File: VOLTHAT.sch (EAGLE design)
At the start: 25 parts, among them IC2 EUP3476SO08T, J1 DC IN

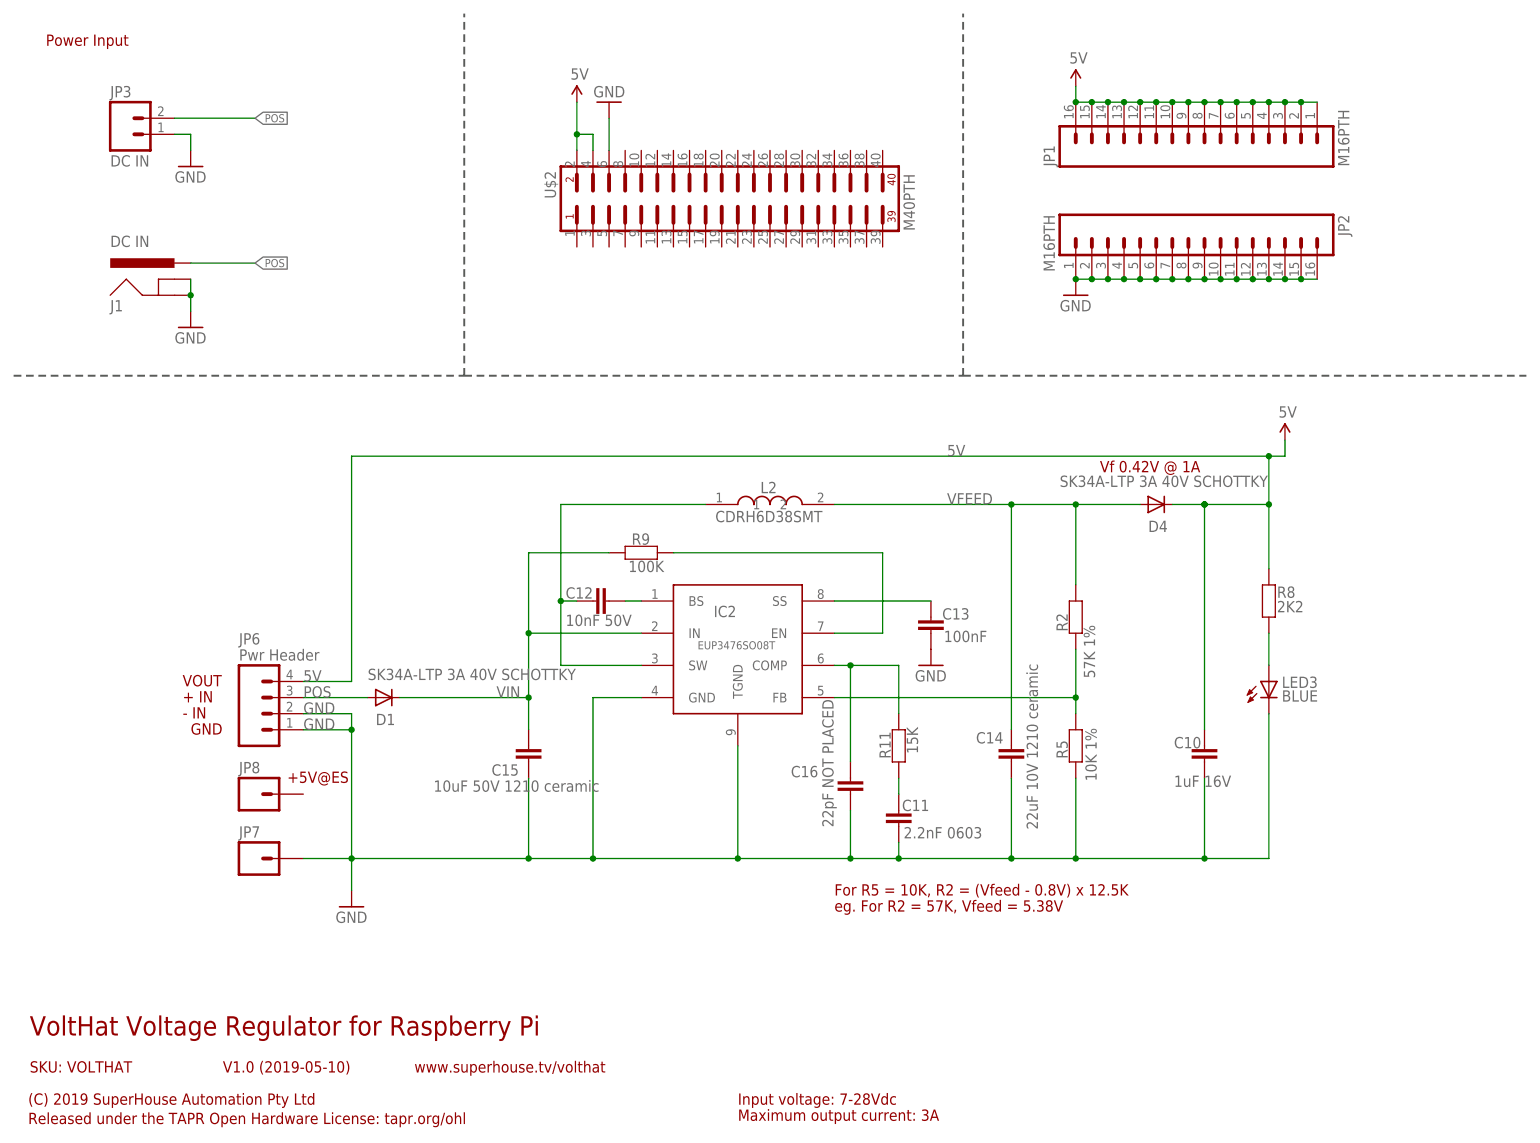
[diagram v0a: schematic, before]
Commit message: Added header to take power from PoE on Raspberry Pi 3 B+
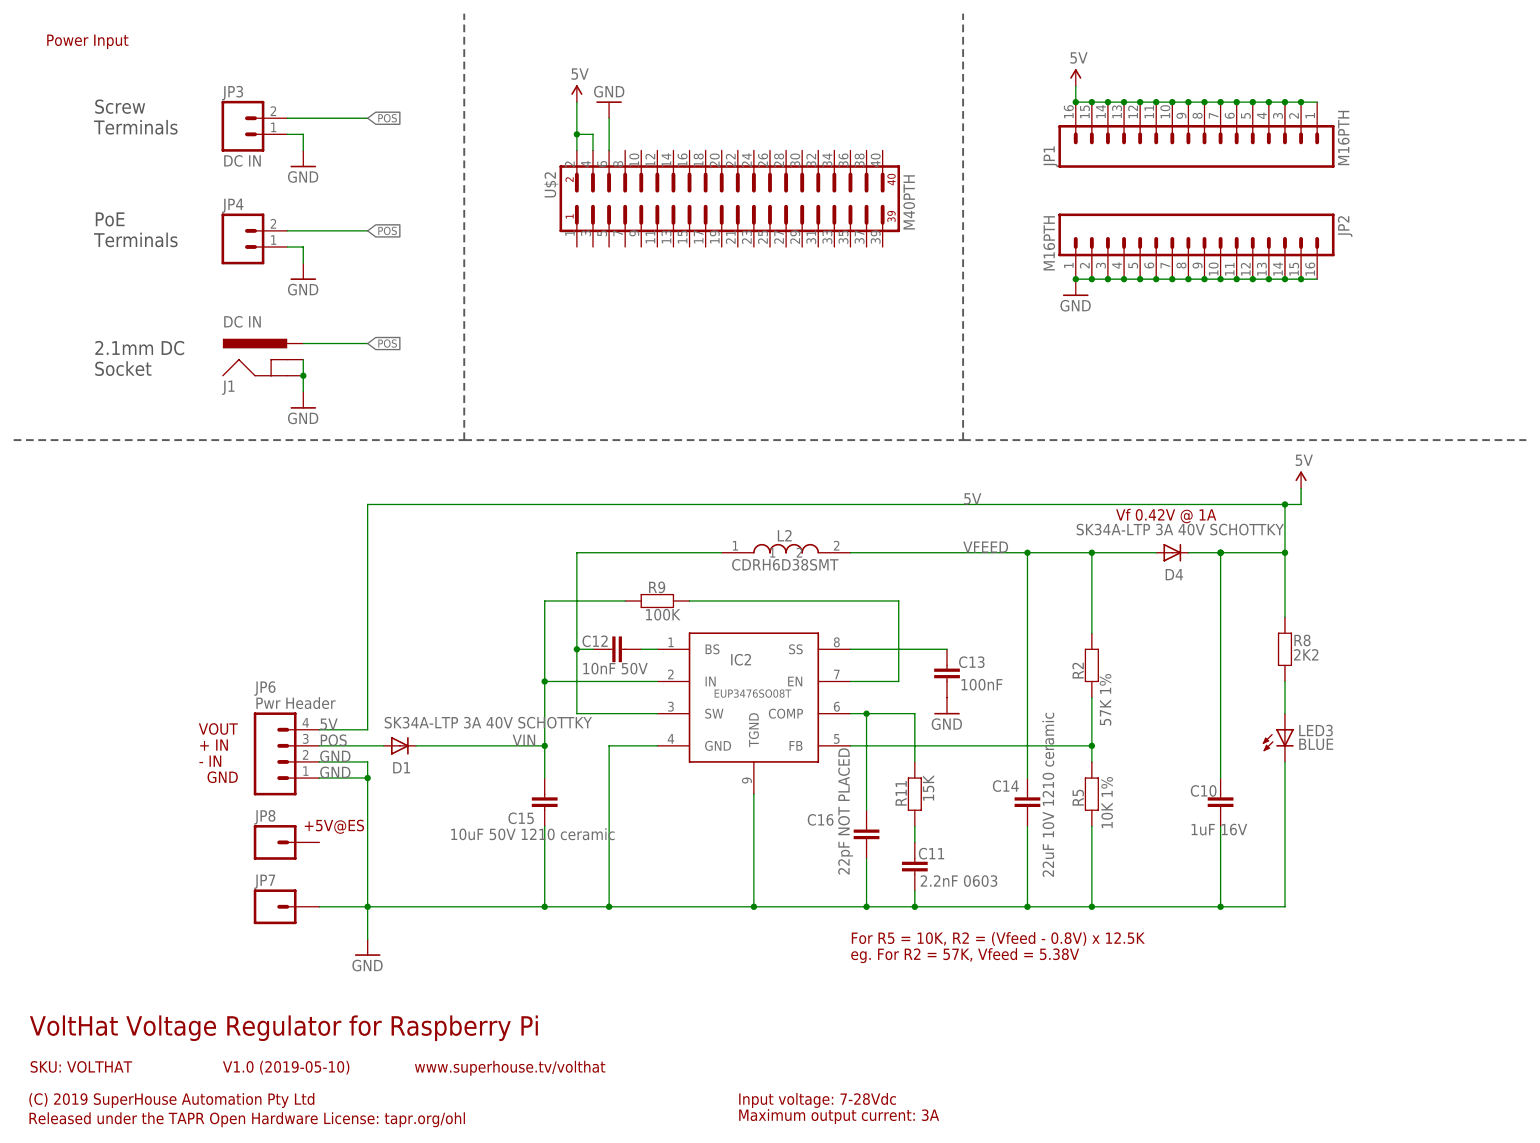
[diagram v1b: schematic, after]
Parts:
- added JP4: (no value), freetronics-jon:M02PTH
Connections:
- net GND: now also JP4.1
- net POS: now also JP4.2
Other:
- note added: "2.1mm DC Socket"
- note added: "PoE Terminals"
- note added: "Screw Terminals"
- moved on the sheet: C10, C11, C12, C13, C14, C15, C16, D1, D4, IC2, J1, JP3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

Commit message: Major routing for v1.0 release
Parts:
- removed JP2: M16PTH, freetronics-jon:M16PTH
- added JP10: OLED, freetronics-jon:M04PTH
- added JP9: M14PTH, freetronics-jon:M14PTH
- added SJ1, SJ2: (no value), freetronics-jon:SJN
- JP1: value M16PTH -> M14PTH; device freetronics-jon:M16PTH -> freetronics-jon:M14PTH
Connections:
- new net 3.3V: JP10.3, U$2.1
- new net N$1: JP4.1, SJ2.1
- new net N$2: JP4.2, SJ1.1
- new net SCL: JP10.2, U$2.5
- new net SDA: JP10.1, U$2.3
- net 5V: now also JP9.1, JP9.10, JP9.11, JP9.12, JP9.13, JP9.14, JP9.2, JP9.3, JP9.4, JP9.5, JP9.6, JP9.7, JP9.8, JP9.9; no longer JP1.1, JP1.10, JP1.11, JP1.12, JP1.13, JP1.14, JP1.15, JP1.16, JP1.2, JP1.3, JP1.4, JP1.5, JP1.6, JP1.7, JP1.8, JP1.9
- net GND: now also JP1.1, JP1.10, JP1.11, JP1.12, JP1.13, JP1.14, JP1.2, JP1.3, JP1.4, JP1.5, JP1.6, JP1.7, JP1.8, JP1.9, JP10.4, SJ2.2, U$2.14, U$2.20, U$2.25, U$2.30, U$2.39, U$2.9; no longer JP2.1, JP2.10, JP2.11, JP2.12, JP2.13, JP2.14, JP2.15, JP2.16, JP2.2, JP2.3, JP2.4, JP2.5, JP2.6, JP2.7, JP2.8, JP2.9, JP4.1
- net POS: now also SJ1.2; no longer JP4.2
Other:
- note added: "I2C OLED Header"
- note added: "PoE Header"
- note added: "Power Rails"
- note added: "Raspberry Pi Header"
- note added: "Voltage Regulator"
- note removed: "PoE Terminals"
- moved on the sheet: C10, C11, C12, C13, C14, C15, C16, D1, D4, IC2, J1, JP3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

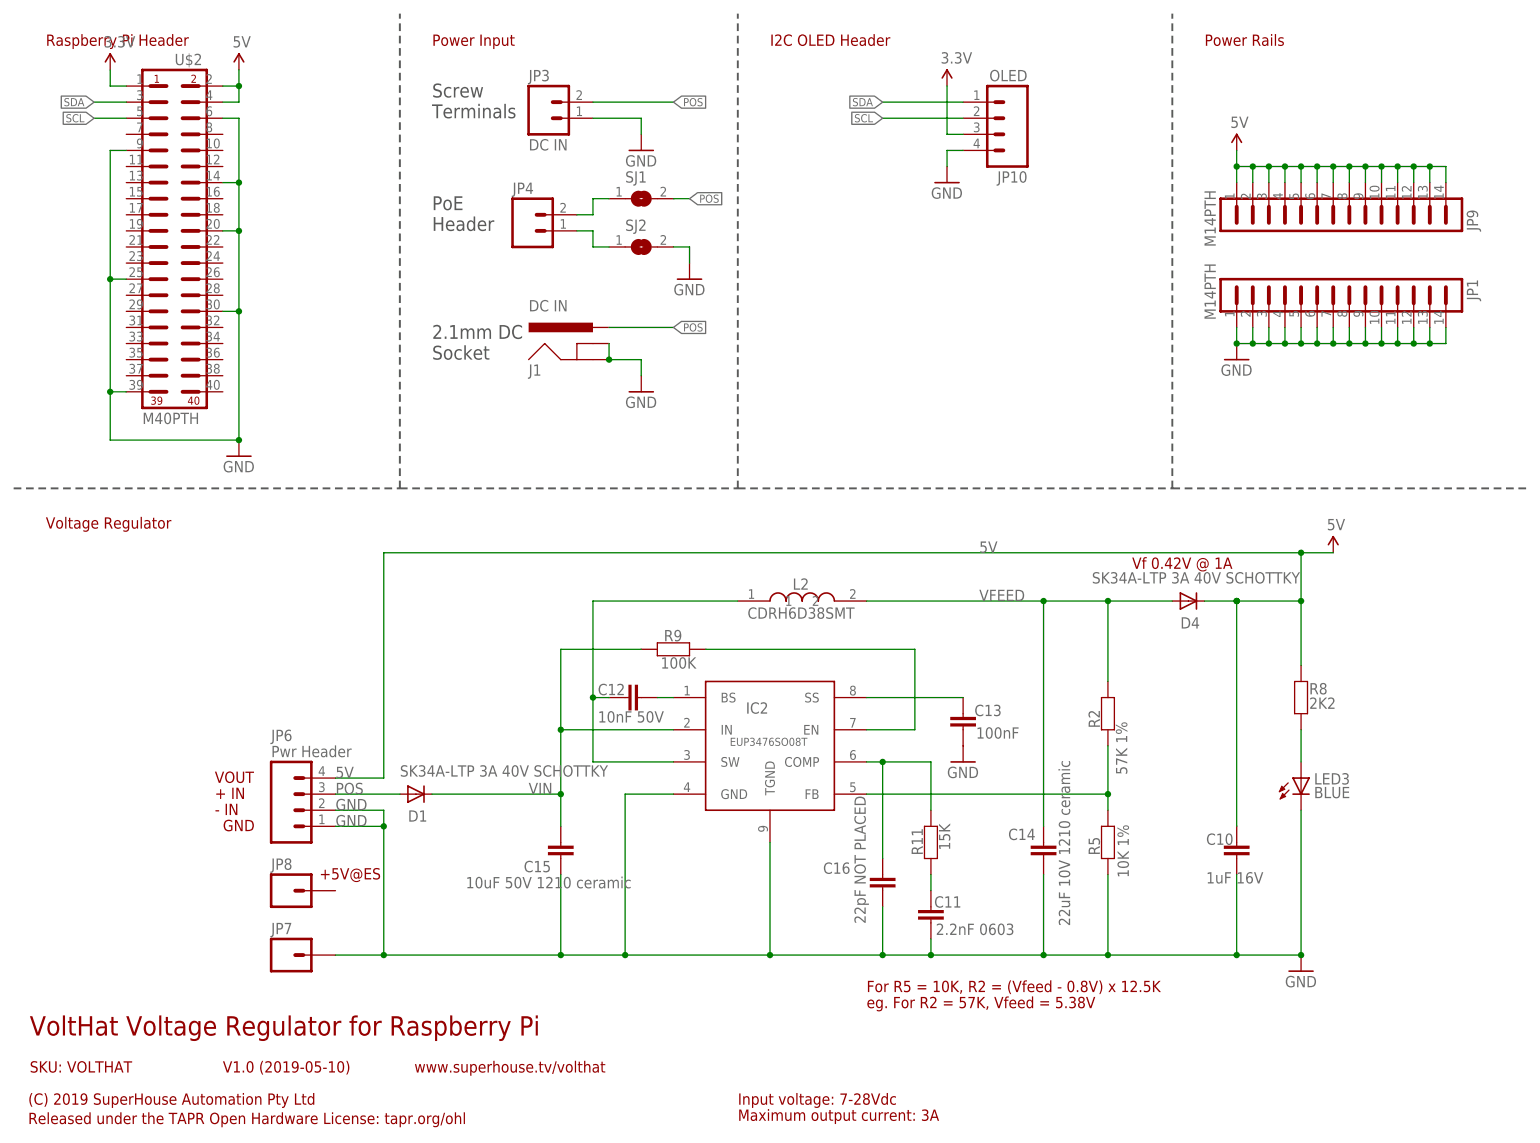
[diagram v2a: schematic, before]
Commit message: Major rework with 3A regulator module for v2.0 release
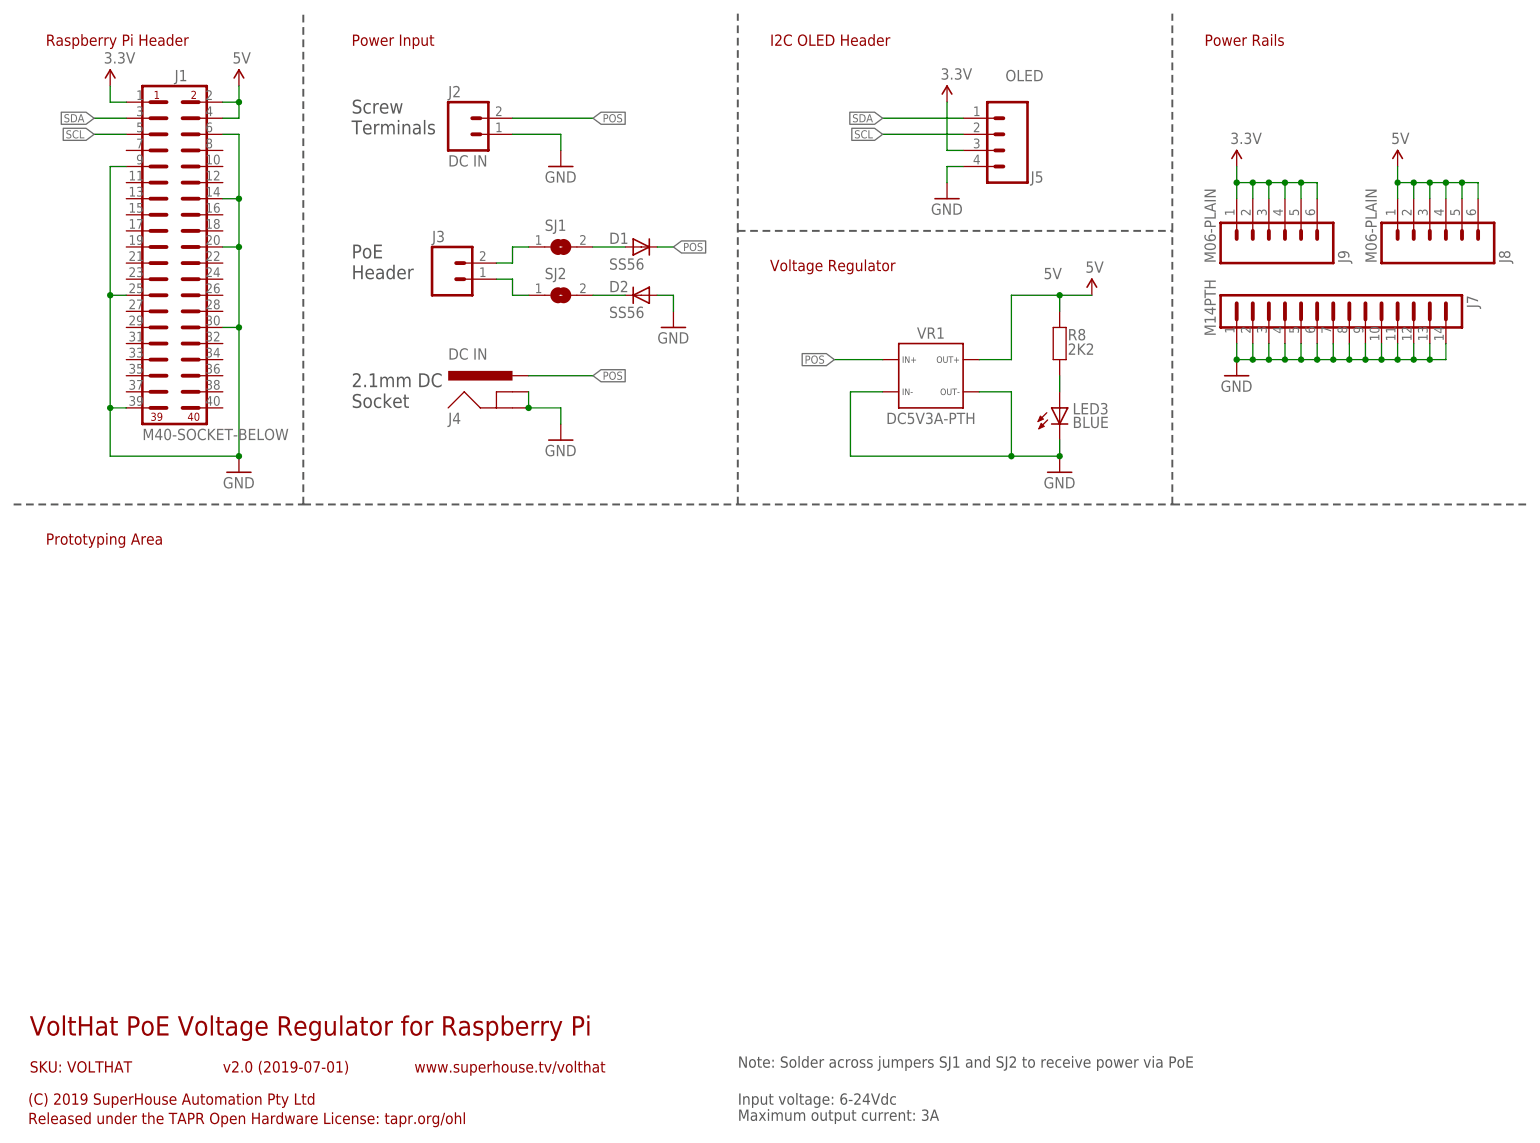
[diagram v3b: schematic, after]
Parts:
- removed C10: 1uF 16V, freetronics:CAP0603
- removed C11: 2.2nF 0603, freetronics-marc:CAP0603
- removed C12: 10nF 50V, freetronics-marc:CAP0603
- removed C13: 100nF, freetronics-marc:CAP0603
- removed C14: 22uF 10V 1210 ceramic, freetronics-jon:C-EUC1210
- removed C15: 10uF 50V 1210 ceramic, freetronics-jon:C-EUC1210
- removed C16: 22pF NOT PLACED, freetronics-marc:CAP0603
- removed D4: SK34A-LTP 3A 40V SCHOTTKY, freetronics-master-v1:DIODESMA
- removed IC2: EUP3476SO08T, freetronics-jon:EUP3476SO08T
- removed JP1, JP9: M14PTH, freetronics-jon:M14PTH
- removed JP10: OLED, freetronics-jon:M04PTH
- removed JP3: DC IN, freetronics-jon:M023.5MM
- removed JP4: (no value), freetronics-jon:M02PTH
- removed JP6: Pwr Header, freetronics:M04PTH
- removed JP7, JP8: M01PTH, freetronics:M01PTH
- removed L2: CDRH6D38SMT, freetronics-jon:CDRH6D38SMT
- removed R11: 15K, freetronics-marc:RESISTOR0603
- removed R2: 57K 1%, freetronics-marc:RESISTOR0603
- removed R5: 10K 1%, freetronics-marc:RESISTOR0603
- removed R9: 100K, freetronics-marc:RESISTOR0603
- removed U$2: M40PTH, freetronics-jon:M40PTH
- added D2: SS56, SuperHouse-DiscreteSemi:DIODESMA
- added J2: DC IN, SuperHouse-Connectors:M02-SCREW-3.5MM
- added J3: (no value), SuperHouse-Connectors:M02-SOCKET-BELOW
- added J4: DC IN, SuperHouse-Connectors:POWER_JACK-SLOTS
- added J5: OLED, SuperHouse-Connectors:M04-PLAIN
- added J7: M14PTH, freetronics-jon:M14PTH
- added J8, J9: M06-PLAIN, SuperHouse-Connectors:M06-PLAIN
- added VR1: DC5V3A-PTH, SuperHouse-Regulators:DC5V3A-PTH
- D1: value SK34A-LTP 3A 40V SCHOTTKY -> SS56; device freetronics-master-v1:DIODESMA -> SuperHouse-DiscreteSemi:DIODESMA
- J1: value DC IN -> M40-SOCKET-BELOW; device freetronics-jon:POWER_JACKPTH_SLOTS -> SuperHouse-Connectors:M40-SOCKET-BELOW
- LED3: device freetronics:LED0603 -> SuperHouse-LEDs:LED0603
- R8: device freetronics:RESISTOR0603 -> SuperHouse-DiscreteSemi:RESISTOR0603
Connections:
- removed net N$204: IC2.EN, R9.1
- removed net N$205: IC2.FB, R2.2, R5.2
- removed net N$206: C16.1, IC2.COMP, R11.2
- removed net N$207: C11.1, R11.1
- removed net N$208: C12.2, IC2.BS
- removed net N$209: C13.2, IC2.SS
- removed net N$210: C12.1, IC2.SW, L2.1
- removed net VFEED: C14.1, D4.A, L2.2, R2.1
- removed net VIN: C15.1, D1.C, IC2.IN, R9.2
- new net N$24: D1.A, SJ1.2
- new net N$25: D2.C, SJ2.2
- net 3.3V: now also J1.1, J5.3, J9.1, J9.2, J9.3, J9.4, J9.5, J9.6; no longer JP10.3, U$2.1
- net 5V: now also J1.2, J1.4, J8.1, J8.2, J8.3, J8.4, J8.5, J8.6, VR1.3; no longer C10.1, D4.C, JP6.4, JP9.1, JP9.10, JP9.11, JP9.12, JP9.13, JP9.14, JP9.2, JP9.3, JP9.4, JP9.5, JP9.6, JP9.7, JP9.8, JP9.9, U$2.2, U$2.4
- net GND: now also D2.A, J1.14, J1.20, J1.25, J1.30, J1.39, J1.6, J1.9, J2.1, J4.GND, J4.GNDBREAK, J5.4, J7.1, J7.10, J7.11, J7.12, J7.13, J7.14, J7.2, J7.3, J7.4, J7.5, J7.6, J7.7, J7.8, J7.9, VR1.1, VR1.4; no longer C10.2, C11.2, C13.1, C14.2, C15.2, C16.2, IC2.GND, IC2.TGND, J1.GND, J1.GNDBREAK, JP1.1, JP1.10, JP1.11, JP1.12, JP1.13, JP1.14, JP1.2, JP1.3, JP1.4, JP1.5, JP1.6, JP1.7, JP1.8, JP1.9, JP10.4, JP3.1, JP6.1, JP6.2, JP7.1, R5.1, SJ2.2, U$2.14, U$2.20, U$2.25, U$2.30, U$2.39, U$2.6, U$2.9
- net N$1: now also J3.1; no longer JP4.1
- net N$2: now also J3.2; no longer JP4.2
- net POS: now also D1.C, J2.2, J4.PWR, VR1.2; no longer D1.A, J1.PWR, JP3.2, JP6.3, SJ1.2
- net SCL: now also J1.5, J5.2; no longer JP10.2, U$2.5
- net SDA: now also J1.3, J5.1; no longer JP10.1, U$2.3
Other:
- note added: "Input voltage: 6-24Vdc"
- note added: "Note: Solder across jumpers SJ1 and SJ2 to receive power via PoE"
- note added: "Prototyping Area"
- note added: "VoltHat PoE Voltage Regulator for Raspberry Pi"
- note added: "v2.0 (2019-07-01)"
- note removed: "+ IN"
- note removed: "+5V@ES"
- note removed: "- IN"
- note removed: "For R5 = 10K, R2 = (Vfeed - 0.8V) x 12.5K"
- note removed: "GND"
- note removed: "Input voltage: 7-28Vdc"
- note removed: "V1.0 (2019-05-10)"
- note removed: "VOUT"
- note removed: "Vf 0.42V @ 1A"
- note removed: "VoltHat Voltage Regulator for Raspberry Pi"
- note removed: "eg. For R2 = 57K, Vfeed = 5.38V"
- moved on the sheet: D1, LED3, R8, SJ1, SJ2
